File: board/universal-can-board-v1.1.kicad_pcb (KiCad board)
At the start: 2 copper layers, 49.3 x 59.4 mm, 79 parts, among them IC1 ATMEGA328P-A, P1 USB_OTG, P2 CONN_01X08, P3 CONN_01X02, P4 CONN_01X08, P5 CONN_01X08, SW1 SW_Push, U1 FT232RL, U2 LM1117-3.3, U3 MCP2515-I/ST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

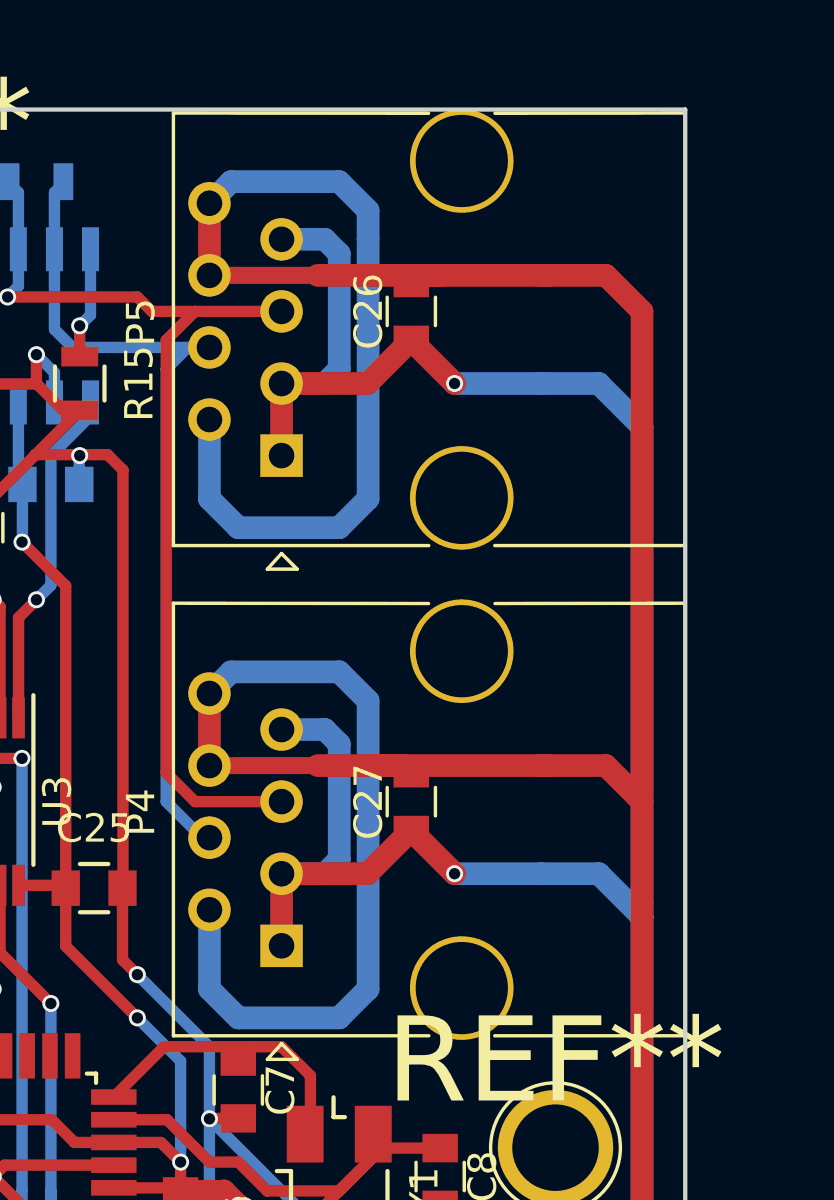
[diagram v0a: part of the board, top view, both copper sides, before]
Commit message: Flipped input filter C (CAN) from top to bottom.
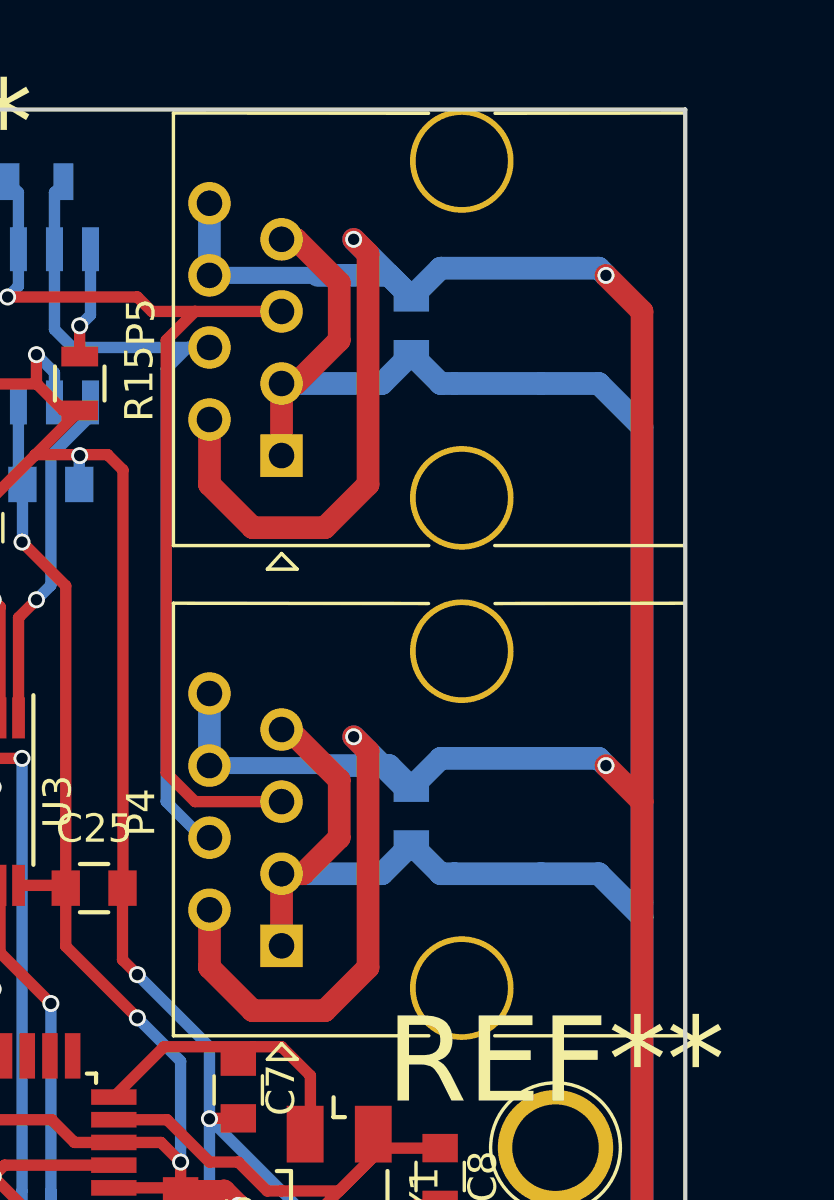
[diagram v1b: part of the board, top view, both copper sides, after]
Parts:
- C26, C27: moved to B.Cu
- moved C26 0.51 mm to (160.5, 58.4)
- moved C27 0.51 mm to (160.5, 75.7)
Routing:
- net GND: track 400.0 -> 386.5 mm, vias 18 -> 22
- net Net-(C26-Pad1): track 107.2 -> 104.0 mm, vias 3 -> 1
